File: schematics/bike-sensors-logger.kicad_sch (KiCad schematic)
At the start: 7 parts, among them J1 MMCX, J2 OBD II

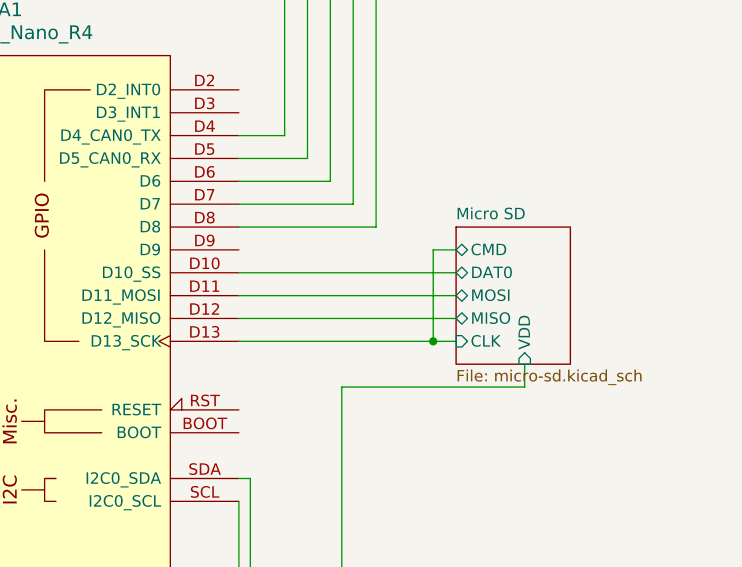
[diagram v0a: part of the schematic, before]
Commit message: Fix micro sd connector wiring
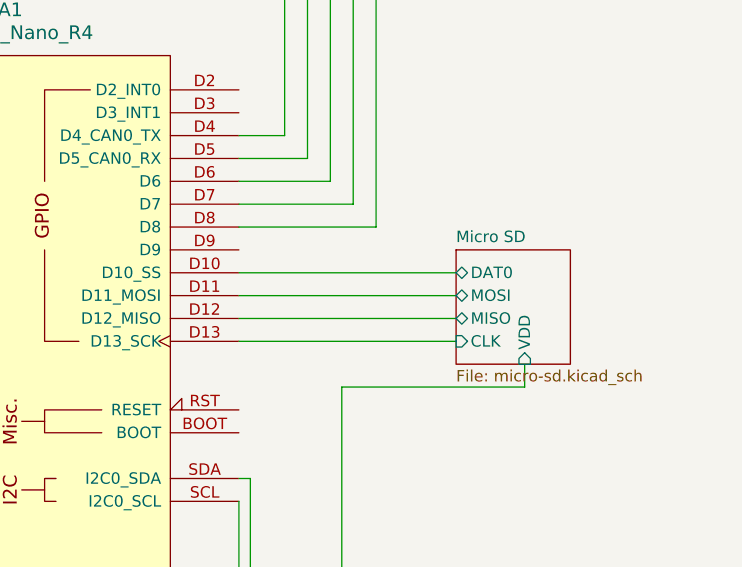
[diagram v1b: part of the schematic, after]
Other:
- sheet Micro SD ports: added none; removed CMD
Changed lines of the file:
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@@
-	)
-	(junction
-		(at 223.52 82.55)
-		(diameter 0)
-		(color 0 0 0 0)
 	)
 	(junction
@@
 	(wire
 		(pts
-			(xy 223.52 82.55) (xy 226.06 82.55)
+			(xy 201.93 82.55) (xy 226.06 82.55)
 		)
 		(stroke
@@
 	(wire
 		(pts
-			(xy 201.93 82.55) (xy 223.52 82.55)
-		)
-		(stroke
-			(width 0)
-			(type default)
-		)
-	)
-	(wire
-		(pts
 			(xy 146.05 110.49) (xy 146.05 147.32)
 		)
@@
 		(pts
 			(xy 128.27 149.86) (xy 147.32 149.86)
-		)
-		(stroke
-			(width 0)
-			(type default)
-		)
-	)
-	(wire
-		(pts
-			(xy 226.06 72.39) (xy 223.52 72.39)
-		)
-		(stroke
-			(width 0)
-			(type default)
-		)
-	)
-	(wire
-		(pts
-			(xy 223.52 72.39) (xy 223.52 82.55)
 		)
 		(stroke
@@
 	)
 	(sheet
-		(at 226.06 69.85)
-		(size 12.7 15.24)
+		(at 226.06 72.39)
+		(size 12.7 12.7)
 		(exclude_from_sim no)
 		(in_bom yes)
@@
 		)
 		(property "Sheetname" "Micro SD"
-			(at 226.06 69.1384 0)
+			(at 226.06 71.6784 0)
 			(effects
 				(font
@@
 			(effects
 				(font
-					(size 1.27 1.27)
-				)
-				(justify left)
-			)
-		)
-		(pin "CMD" bidirectional
-			(at 226.06 72.39 180)
-			(effects
-				(font

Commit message: Buck name fix
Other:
- sheet 12V to 5V + 3.3V buck renamed 12V to 5V + 3.3V bucks
- sheet 12V to 5V + 3.3V bucks: file down-step-buck-converters.kicad_sch -> step-down-buck-converters.kicad_sch
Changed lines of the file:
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@@
 			(color 0 0 0 0.0000)
 		)
-		(property "Sheetname" "12V to 5V + 3.3V buck"
+		(property "Sheetname" "12V to 5V + 3.3V bucks"
 			(at 97.79 69.1384 0)
 			(effects
@@
 			)
 		)
-		(property "Sheetfile" "down-step-buck-converters.kicad_sch"
+		(property "Sheetfile" "step-down-buck-converters.kicad_sch"
 			(at 97.79 80.5946 0)
 			(effects

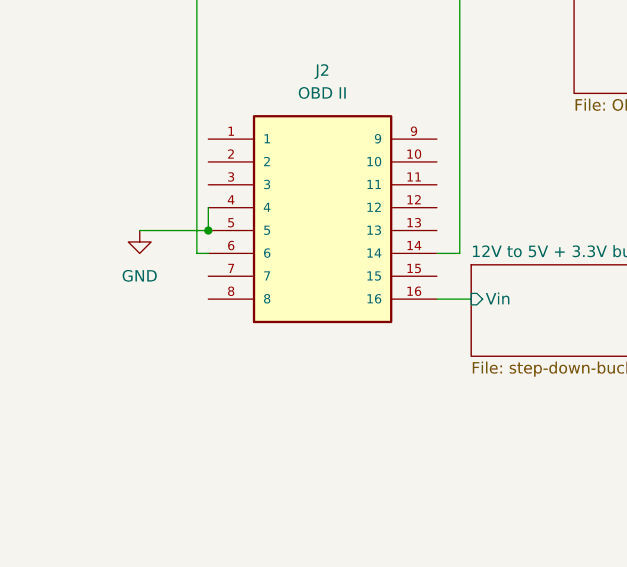
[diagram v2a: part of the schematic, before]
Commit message: Removed useless GND link from the OBD II port and added a note about power source
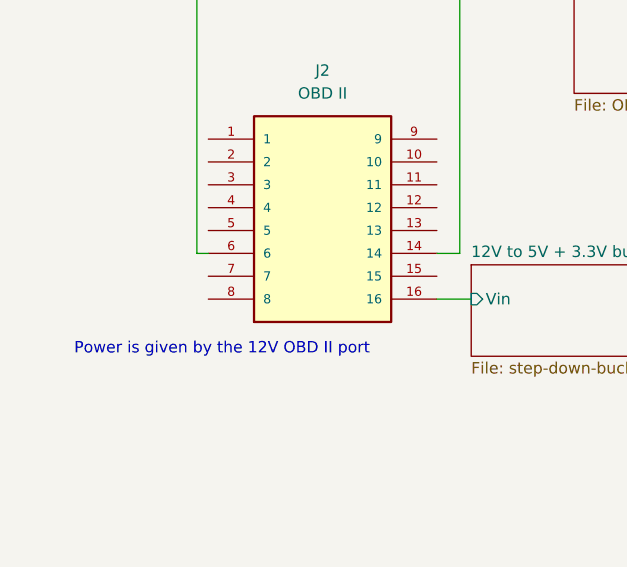
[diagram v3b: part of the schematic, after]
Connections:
- net GND: no longer J2.4, J2.5
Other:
- note added: "Power is given by the 12V OBD II port"
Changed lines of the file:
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@@
 		(title "Bike sensors logger MK1")
+	)
+	(text "Power is given by the 12V OBD II port"
+		(exclude_from_sim no)
+		(at 70.104 79.248 0)
+		(effects
+			(font
+				(size 1.27 1.27)
+			)
+		)
 	)
 	(junction
@@
 	)
 	(junction
-		(at 68.58 66.04)
-		(diameter 0)
-		(color 0 0 0 0)
-	)
-	(junction
 		(at 147.32 111.76)
 		(diameter 0)
@@
 	(wire
 		(pts
-			(xy 68.58 63.5) (xy 68.58 66.04)
-		)
-		(stroke
-			(width 0)
-			(type default)
-		)
-	)
-	(wire
-		(pts
 			(xy 119.38 110.49) (xy 146.05 110.49)
 		)
@@
 		(pts
 			(xy 139.7 95.25) (xy 139.7 135.89)
-		)
-		(stroke
-			(width 0)
-			(type default)
-		)
-	)
-	(wire
-		(pts
-			(xy 60.96 66.04) (xy 68.58 66.04)
 		)
 		(stroke
@@
 					(unit 1)
 				)
-			)
-		)
-	)
-	(symbol
-		(lib_id "power:GND")
-		(at 60.96 66.04 0)
-		(unit 1)
-		(exclude_from_sim no)
-		(in_bom yes)
-		(on_board yes)
-		(dnp no)
-		(fields_autoplaced yes)
-		(property "Reference" "#PWR04"
-			(at 60.96 72.39 0)
-			(effects
-				(font
-					(size 1.27 1.27)
-				)
-				(hide yes)
-			)
-		)
-		(property "Value" "GND"
-			(at 60.96 71.12 0)
-			(effects
-				(font
-					(size 1.27 1.27)
-				)
-			)
-		)
-		(property "Footprint" ""
-			(at 60.96 66.04 0)
-			(effects
-				(font
-					(size 1.27 1.27)
-				)
-				(hide yes)
-			)
-		)
-		(property "Datasheet" ""
-			(at 60.96 66.04 0)
-			(effects
-				(font
-					(size 1.27 1.27)
-				)
-				(hide yes)
-			)
-		)
-		(property "Description" "Power symbol creates a global label with name \"GND\" , ground"
-			(at 60.96 66.04 0)
-			(effects
-				(font
-					(size 1.27 1.27)
-				)
-				(hide yes)
-			)
-		)
-		(pin "1"
-		)
-		(instances
-			(project ""
-				(path "/2c1d9222-af16-428b-85a5-a3d420373d70"
-					(reference "#PWR04")
-					(unit 1)
-				)
